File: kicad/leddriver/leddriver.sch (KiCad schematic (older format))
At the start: 7 parts, among them J1 Conn_01x02_Male, J2 Conn_01x01_Male, U1 TLC555xP

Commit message: Add new code
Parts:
- removed J1: Conn_01x02_Male, Connector_PinSocket_2.54mm:PinSocket_1x02_P2.54mm_Vertical, symbol Connector:Conn_01x02_Male
- removed J2: Conn_01x01_Male, Connector_PinHeader_2.54mm:PinHeader_1x01_P2.54mm_Vertical, symbol Connector:Conn_01x01_Male
- added BZ1: Buzzer, Buzzer_Beeper:MagneticBuzzer_ProSignal_ABI-010-RC, symbol Device:Buzzer
- added C3: 4.7uF, Capacitor_THT:C_Disc_D4.3mm_W1.9mm_P5.00mm, symbol Device:C
- added C4: .01uF, Capacitor_THT:C_Disc_D4.3mm_W1.9mm_P5.00mm, symbol Device:C
- added J1, J3: Conn_01x01_Male, Connector_PinHeader_2.54mm:PinHeader_1x01_P2.54mm_Vertical, symbol Connector:Conn_01x01_Male
- added J2: Conn_01x02_Male, Connector_PinSocket_2.54mm:PinSocket_1x02_P2.54mm_Vertical, symbol Connector:Conn_01x02_Male
- added Q1: 2N3904, leddriver:TO-92_HandSolder_Large_Pad, symbol Transistor_BJT:2N3904
- added R3, R5: 68k, Resistor_THT:R_Axial_DIN0204_L3.6mm_D1.6mm_P2.54mm_Vertical, symbol Device:R
- added R4: 1k, Resistor_THT:R_Axial_DIN0204_L3.6mm_D1.6mm_P2.54mm_Vertical, symbol Device:R
- added SW1: SW_Push, Button_Switch_THT:SW_PUSH_6mm_H5mm, symbol Switch:SW_Push
- added U2: TLC555xP, Package_DIP:DIP-8_W7.62mm, symbol Timer:TLC555xP
- C1: value 0.01uF -> 1uF; footprint Capacitor_SMD:C_1206_3216Metric_Pad1.33x1.80mm_HandSolder -> Capacitor_THT:C_Disc_D4.3mm_W1.9mm_P5.00mm
- C2: value 10uF -> .01uF; footprint Capacitor_SMD:C_1206_3216Metric_Pad1.33x1.80mm_HandSolder -> Capacitor_THT:C_Disc_D4.3mm_W1.9mm_P5.00mm
- R1, R2: footprint Resistor_SMD:R_0805_2012Metric_Pad1.20x1.40mm_HandSolder -> Resistor_THT:R_Axial_DIN0204_L3.6mm_D1.6mm_P2.54mm_Vertical
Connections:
- net GND: now also BZ1.2 (+), C3.2, C4.2, J2.2 (Pin_2), R3.2, U2.1 (GND)
- net VCC: now also R2.1, J2.1 (Pin_1), J3.1 (Pin_1), Q1.3 (C), R4.1, U2.8 (VCC)
- net at R2.2, U1.2 (TR), U1.6 (THR): now also R3.1, SW1.2; no longer C2.1
- net OUT1: now reaches U1.3 (Q)
- net OUT1: now also U2.4 (R)
- net at U1.5 (CV): now also C2.1; no longer C1.1
- new net: C1.1, R1.2, SW1.1
- new net: C3.1, R5.2, U2.2 (TR), U2.6 (THR)
- new net: C4.1, U2.5 (CV)
- new net: R4.2, R5.1, U2.7 (DIS)
- new net: BZ1.1 (-), Q1.1 (E)
- new net OUT: J1.1 (Pin_1), Q1.2 (B), U2.3 (Q)
- now unconnected: U1.7 (DIS)
- no-connect marks 0 -> 1
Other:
- moved on the sheet: U1

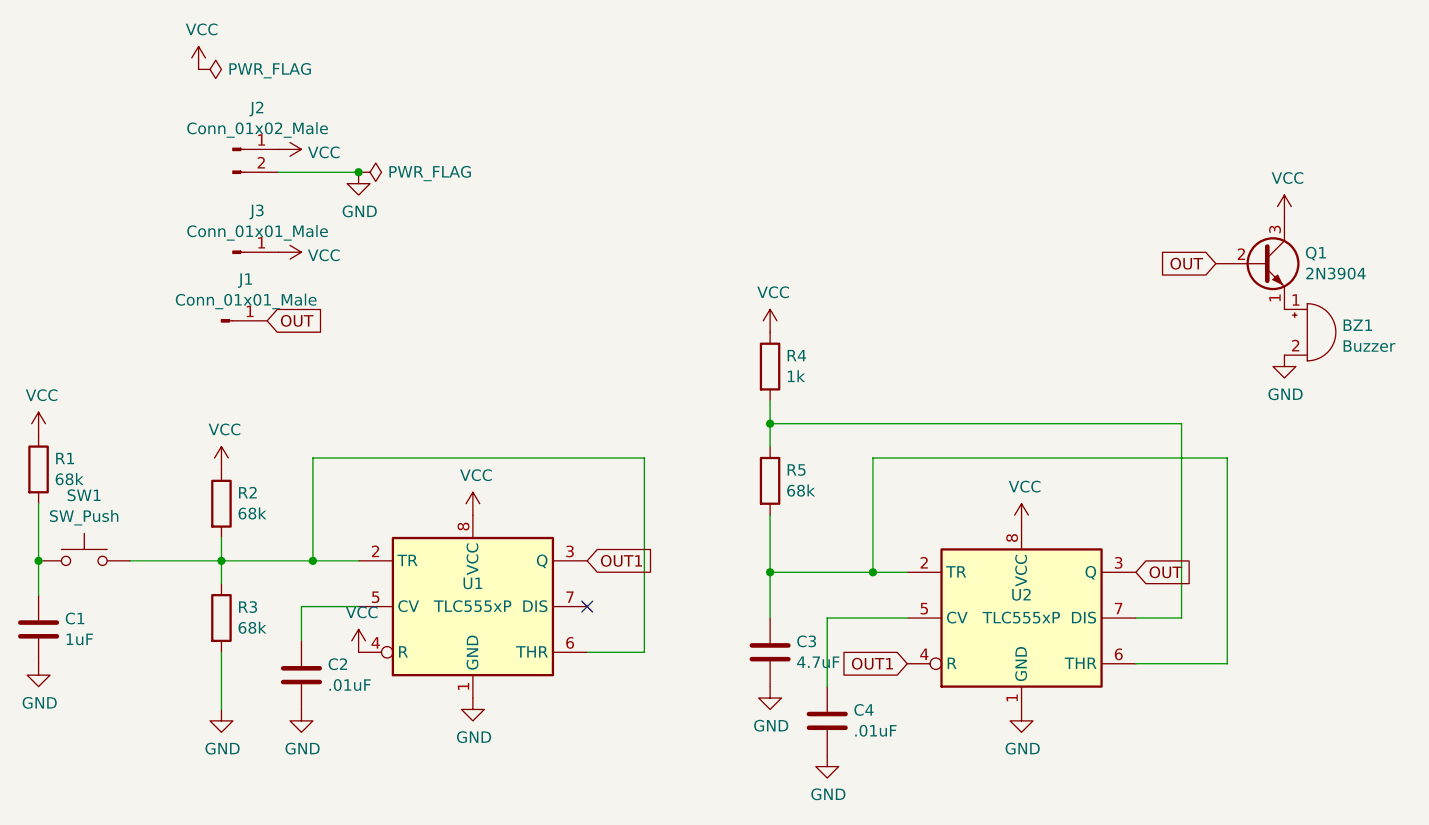
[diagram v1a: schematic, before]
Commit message: Add new led driver schematic
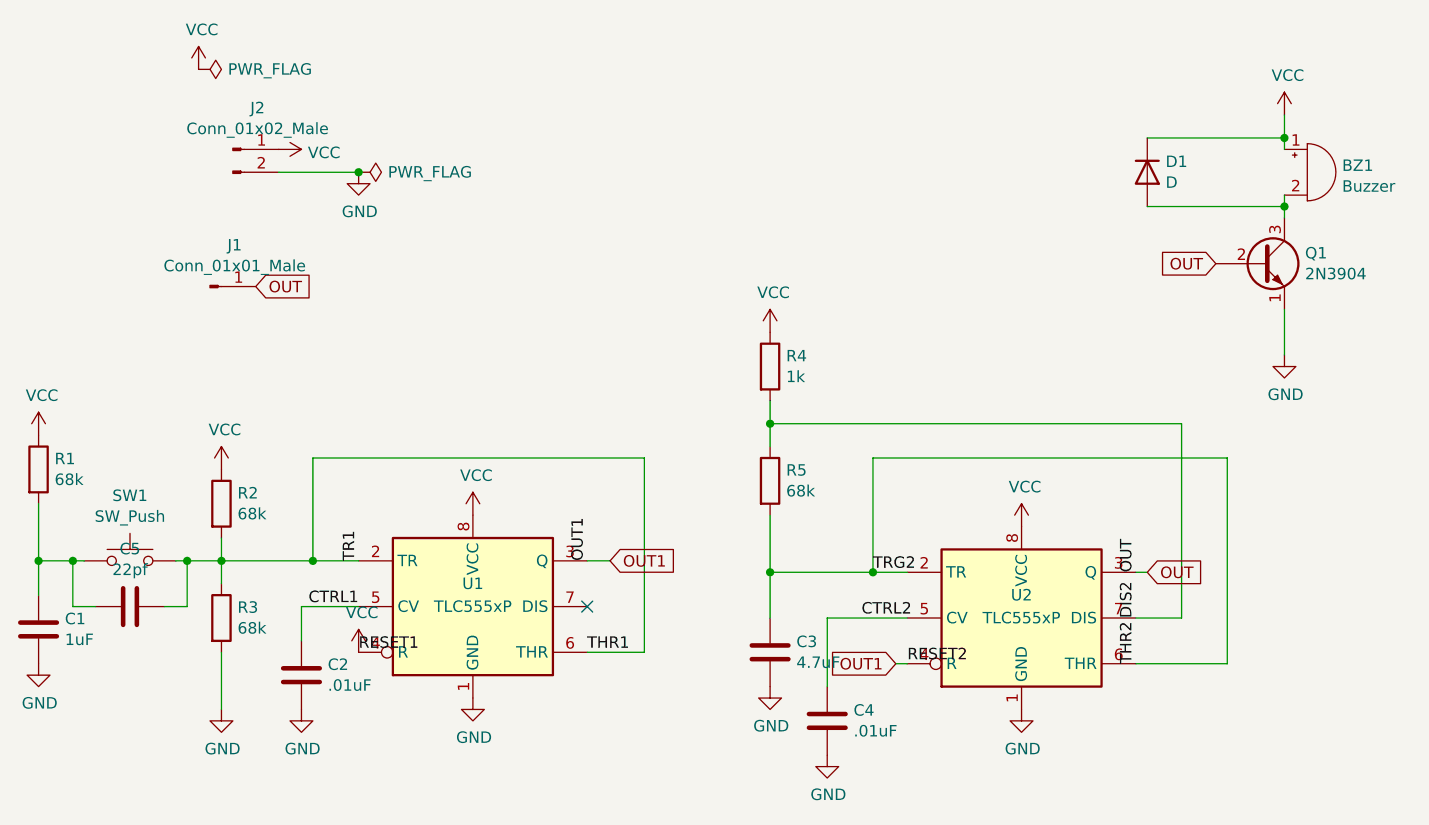
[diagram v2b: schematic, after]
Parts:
- removed J3: Conn_01x01_Male, Connector_PinHeader_2.54mm:PinHeader_1x01_P2.54mm_Vertical, symbol Connector:Conn_01x01_Male
- added C5: 22pf, Capacitor_THT:C_Disc_D3.0mm_W1.6mm_P2.50mm, symbol Device:C
- added D1: D, Diode_THT:D_5KPW_P7.62mm_Vertical_AnodeUp, symbol Device:D
- C1, C2, C3, C4: footprint Capacitor_THT:C_Disc_D4.3mm_W1.9mm_P5.00mm -> Capacitor_THT:C_Radial_D4.0mm_H5.0mm_P1.50mm
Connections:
- net GND: now also Q1.1 (E); no longer BZ1.2 (+)
- net VCC: now also BZ1.1 (-), D1.1 (K); no longer Q1.3 (C)
- net THR1: now reaches R2.2, R3.1, SW1.2, U1.2 (TR), U1.6 (THR)
- net THR1: now also C5.1
- net CTRL1: now reaches C2.1, U1.5 (CV)
- net at C1.1, R1.2, SW1.1: now also C5.2
- net THR2: now reaches C3.1, R5.2, U2.2 (TR), U2.6 (THR)
- net CTRL2: now reaches C4.1, U2.5 (CV)
- net DIS2: now reaches R4.2, R5.1, U2.7 (DIS)
- new net: BZ1.2 (+), D1.2 (A), Q1.3 (C)
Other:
- moved on the sheet: BZ1, J1, SW1
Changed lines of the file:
@@
 F 0 "C1" H 3765 3246 50  0000 L CNN
 F 1 "1uF" H 3765 3155 50  0000 L CNN
-F 2 "Capacitor_THT:C_Disc_D4.3mm_W1.9mm_P5.00mm" H 3688 3050 50  0001 C CNN
+F 2 "Capacitor_THT:C_Radial_D4.0mm_H5.0mm_P1.50mm" H 3688 3050 50  0001 C CNN
 F 3 "~" H 3650 3200 50  0001 C CNN
 	1    3650 3200
@@
 Wire Wire Line
 	4450 2900 4450 3000
-Wire Wire Line
-	4450 2900 4850 2900
 Connection ~ 4850 2900
 $Comp
@@
 Wire Wire Line
 	4700 1200 5050 1200
-Text GLabel 4650 1850 2    50   Input ~ 0
+Text GLabel 4600 1700 2    50   Input ~ 0
 OUT
-Text GLabel 6050 2900 2    50   Input ~ 0
+Text GLabel 6150 2900 2    50   Input ~ 0
 OUT1
 $Comp
@@
 F 0 "C2" H 4915 3446 50  0000 L CNN
 F 1 ".01uF" H 4915 3355 50  0000 L CNN
-F 2 "Capacitor_THT:C_Disc_D4.3mm_W1.9mm_P5.00mm" H 4838 3250 50  0001 C CNN
+F 2 "Capacitor_THT:C_Radial_D4.0mm_H5.0mm_P1.50mm" H 4838 3250 50  0001 C CNN
 F 3 "~" H 4800 3400 50  0001 C CNN
 	1    4800 3400
@@
 	1    0    0    -1
 $EndComp
-Text GLabel 7450 3350 0    50   Input ~ 0
+Text GLabel 7400 3350 0    50   Input ~ 0
 OUT1
 $Comp
@@
 F 0 "C3" H 6965 3346 50  0000 L CNN
 F 1 "4.7uF" H 6965 3255 50  0000 L CNN
-F 2 "Capacitor_THT:C_Disc_D4.3mm_W1.9mm_P5.00mm" H 6888 3150 50  0001 C CNN
+F 2 "Capacitor_THT:C_Radial_D4.0mm_H5.0mm_P1.50mm" H 6888 3150 50  0001 C CNN
 F 3 "~" H 6850 3300 50  0001 C CNN
 	1    6850 3300
@@
 F 0 "C4" H 7215 3646 50  0000 L CNN
 F 1 ".01uF" H 7215 3555 50  0000 L CNN
-F 2 "Capacitor_THT:C_Disc_D4.3mm_W1.9mm_P5.00mm" H 7138 3450 50  0001 C CNN
+F 2 "Capacitor_THT:C_Radial_D4.0mm_H5.0mm_P1.50mm" H 7138 3450 50  0001 C CNN
 F 3 "~" H 7100 3600 50  0001 C CNN
 	1    7100 3600
@@
 Wire Wire Line
 	6850 2300 6850 2400
-Text GLabel 8450 2950 2    50   Input ~ 0
+Text GLabel 8500 2950 2    50   Input ~ 0
 OUT
-Wire Wire Line
-	4050 2900 4450 2900
-Connection ~ 3650 2900
-Wire Wire Line
-	3650 2900 3650 3050
-Wire Wire Line
-	3650 2650 3650 2900
-$Comp
-L Switch:SW_Push SW1
-U 1 1 5F8F5FE1
-P 3850 2900
-F 0 "SW1" H 3850 3185 50  0000 C CNN
-F 1 "SW_Push" H 3850 3094 50  0000 C CNN
-F 2 "Button_Switch_THT:SW_PUSH_6mm_H5mm" H 3850 3100 50  0001 C CNN
-F 3 "~" H 3850 3100 50  0001 C CNN
-	1    3850 2900
-	1    0    0    -1
-$EndComp
 $Comp
 L Connector:Conn_01x02_Male J2
@@
 L Connector:Conn_01x01_Male J1
 U 1 1 5F9568D2
-P 4450 1850
-F 0 "J1" H 4558 2031 50  0000 C CNN
-F 1 "Conn_01x01_Male" H 4558 1940 50  0000 C CNN
-F 2 "Connector_PinHeader_2.54mm:PinHeader_1x01_P2.54mm_Vertical" H 4450 1850 50  0001 C CNN
-F 3 "~" H 4450 1850 50  0001 C CNN
-	1    4450 1850
-	1    0    0    -1
-$EndComp
-$Comp
-L Connector:Conn_01x01_Male J3
-U 1 1 5F9649F6
-P 4500 1550
-F 0 "J3" H 4608 1731 50  0000 C CNN
-F 1 "Conn_01x01_Male" H 4608 1640 50  0000 C CNN
-F 2 "Connector_PinHeader_2.54mm:PinHeader_1x01_P2.54mm_Vertical" H 4500 1550 50  0001 C CNN
-F 3 "~" H 4500 1550 50  0001 C CNN
-	1    4500 1550
+P 4400 1700
+F 0 "J1" H 4508 1881 50  0000 C CNN
+F 1 "Conn_01x01_Male" H 4508 1790 50  0000 C CNN
+F 2 "Connector_PinHeader_2.54mm:PinHeader_1x01_P2.54mm_Vertical" H 4400 1700 50  0001 C CNN
+F 3 "~" H 4400 1700 50  0001 C CNN
+	1    4400 1700
 	1    0    0    -1
 $EndComp
@@
 $EndComp
 $Comp
-L power:VCC #PWR0106
-U 1 1 5F97C45E
-P 4700 1550
-F 0 "#PWR0106" H 4700 1400 50  0001 C CNN
-F 1 "VCC" V 4715 1678 50  0000 L CNN
-F 2 "" H 4700 1550 50  0001 C CNN
-F 3 "" H 4700 1550 50  0001 C CNN
-	1    4700 1550
-	0    1    1    0
-$EndComp
-$Comp
 L power:VCC #PWR0107
 U 1 1 5F97F134
@@
 L Device:Buzzer BZ1
 U 1 1 5F996F1B
-P 9200 1900
-F 0 "BZ1" H 9352 1929 50  0000 L CNN
-F 1 "Buzzer" H 9352 1838 50  0000 L CNN
-F 2 "Buzzer_Beeper:MagneticBuzzer_ProSignal_ABI-010-RC" V 9175 2000 50  0001 C CNN
-F 3 "~" V 9175 2000 50  0001 C CNN
-	1    9200 1900
+P 9200 1200
+F 0 "BZ1" H 9352 1229 50  0000 L CNN
+F 1 "Buzzer" H 9352 1138 50  0000 L CNN
+F 2 "Buzzer_Beeper:MagneticBuzzer_ProSignal_ABI-010-RC" V 9175 1300 50  0001 C CNN
+F 3 "~" V 9175 1300 50  0001 C CNN
+	1    9200 1200
 	1    0    0    -1
 $EndComp
@@
 L power:VCC #PWR0114
 U 1 1 5F9A00D1
-P 9100 1400
-F 0 "#PWR0114" H 9100 1250 50  0001 C CNN
-F 1 "VCC" H 9115 1573 50  0000 C CNN
-F 2 "" H 9100 1400 50  0001 C CNN
-F 3 "" H 9100 1400 50  0001 C CNN
-	1    9100 1400
-	1    0    0    -1
-$EndComp
+P 9100 950
+F 0 "#PWR0114" H 9100 800 50  0001 C CNN
+F 1 "VCC" H 9115 1123 50  0000 C CNN
+F 2 "" H 9100 950 50  0001 C CNN
+F 3 "" H 9100 950 50  0001 C CNN
+	1    9100 950
+	1    0    0    -1
+$EndComp
+Text Label 7300 2950 0    50   ~ 0
+TRG2
+Text Label 7250 3150 0    50   ~ 0
+CTRL2
+Wire Wire Line
+	7400 3350 7450 3350
+Text Label 8450 2950 1    50   ~ 0
+OUT
+Wire Wire Line
+	8450 2950 8500 2950
+Text Label 8450 3150 1    50   ~ 0
+DIS2
+Text Label 8450 3350 1    50   ~ 0
+THR2
+Text Label 5050 2900 1    50   ~ 0
+TR1
+Text Label 7450 3350 0    50   ~ 0
+RESET2
+Text Label 5050 3100 2    50   ~ 0
+CTRL1
+Text Label 5050 3300 0    50   ~ 0
+RESET1
+Text Label 6050 3300 0    50   ~ 0
+THR1
+Text Label 6050 2900 1    50   ~ 0
+OUT1
+Wire Wire Line
+	6050 2900 6150 2900
+Wire Wire Line
+	9100 950  9100 1050
+Wire Wire Line
+	9100 1300 9100 1350
+$Comp
+L Device:D D1
+U 1 1 5F93D059
+P 8500 1200
+F 0 "D1" V 8454 1280 50  0000 L CNN
+F 1 "D" V 8545 1280 50  0000 L CNN
+F 2 "Diode_THT:D_5KPW_P7.62mm_Vertical_AnodeUp" H 8500 1200 50  0001 C CNN
+F 3 "~" H 8500 1200 50  0001 C CNN
+	1    8500 1200
+	0    1    1    0
+$EndComp
+Wire Wire Line
+	8500 1350 9100 1350
+Connection ~ 9100 1350
+Wire Wire Line
+	9100 1350 9100 1400
+Wire Wire Line
+	8500 1050 9100 1050
+Connection ~ 9100 1050
+Wire Wire Line
+	9100 1050 9100 1100
+Wire Wire Line
+	9100 1800 9100 2000
+$Comp
+L Device:C C5
+U 1 1 5F94D72B
+P 4050 3100
+F 0 "C5" V 3798 3100 50  0000 C CNN
+F 1 "22pf" V 3889 3100 50  0000 C CNN
+F 2 "Capacitor_THT:C_Disc_D3.0mm_W1.6mm_P2.50mm" H 4088 2950 50  0001 C CNN
+F 3 "~" H 4050 3100 50  0001 C CNN
+	1    4050 3100
+	0    1    1    0
+$EndComp
+Wire Wire Line
+	4450 2900 4850 2900
+$Comp
+L Switch:SW_Push SW1
+U 1 1 5F8F5FE1
+P 4050 2900
+F 0 "SW1" H 4050 3185 50  0000 C CNN
+F 1 "SW_Push" H 4050 3094 50  0000 C CNN
+F 2 "Button_Switch_THT:SW_PUSH_6mm_H5mm" H 4050 3100 50  0001 C CNN
+F 3 "~" H 4050 3100 50  0001 C CNN
+	1    4050 2900
+	1    0    0    -1
+$EndComp
+Wire Wire Line
+	3650 2650 3650 2900
+Wire Wire Line
+	3650 2900 3800 2900
+Connection ~ 3650 2900
+Wire Wire Line
+	3650 2900 3650 3050
+Wire Wire Line
+	4250 2900 4300 2900
+Wire Wire Line
+	4200 3100 4300 3100
+Wire Wire Line
+	4300 3100 4300 2900
+Connection ~ 4300 2900
+Wire Wire Line
+	4300 2900 4450 2900
+Wire Wire Line
+	3900 3100 3800 3100
+Wire Wire Line
+	3800 3100 3800 2900
+Connection ~ 3800 2900
+Wire Wire Line
+	3800 2900 3850 2900
 $EndSCHEMATC

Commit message: Add change according to 12v test
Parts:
- added R6, R7: 10k, Resistor_THT:R_Axial_DIN0204_L3.6mm_D1.6mm_P2.54mm_Vertical, symbol Device:R
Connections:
- net GND: now also R7.2
- net OUT: now also R6.2; no longer Q1.2 (B)
- new net: Q1.2 (B), R6.1, R7.1
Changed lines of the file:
@@
 	1    0    0    -1
 $EndComp
-Text GLabel 8800 1600 0    50   Input ~ 0
+Text GLabel 8000 1600 0    50   Input ~ 0
 OUT
 $Comp
@@
 	9100 1050 9100 1100
 Wire Wire Line
-	9100 1800 9100 2000
+	9100 1800 9100 1950
 $Comp
 L Device:C C5
@@
 Wire Wire Line
 	3800 2900 3850 2900
+$Comp
+L Device:R R7
+U 1 1 5F947F9D
+P 8550 1750
+F 0 "R7" H 8620 1796 50  0000 L CNN
+F 1 "10k" H 8620 1705 50  0000 L CNN
+F 2 "Resistor_THT:R_Axial_DIN0204_L3.6mm_D1.6mm_P2.54mm_Vertical" V 8480 1750 50  0001 C CNN
+F 3 "~" H 8550 1750 50  0001 C CNN
+	1    8550 1750
+	1    0    0    -1
+$EndComp
+$Comp
+L Device:R R6
+U 1 1 5F949B69
+P 8250 1600
+F 0 "R6" V 8043 1600 50  0000 C CNN
+F 1 "10k" V 8134 1600 50  0000 C CNN
+F 2 "Resistor_THT:R_Axial_DIN0204_L3.6mm_D1.6mm_P2.54mm_Vertical" V 8180 1600 50  0001 C CNN
+F 3 "~" H 8250 1600 50  0001 C CNN
+	1    8250 1600
+	0    1    1    0
+$EndComp
+Wire Wire Line
+	8000 1600 8100 1600
+Wire Wire Line
+	8400 1600 8550 1600
+Wire Wire Line
+	8550 1600 8800 1600
+Connection ~ 8550 1600
+Wire Wire Line
+	8550 1900 8550 1950
+Wire Wire Line
+	8550 1950 9100 1950
+Connection ~ 9100 1950
+Wire Wire Line
+	9100 1950 9100 2000
 $EndSCHEMATC

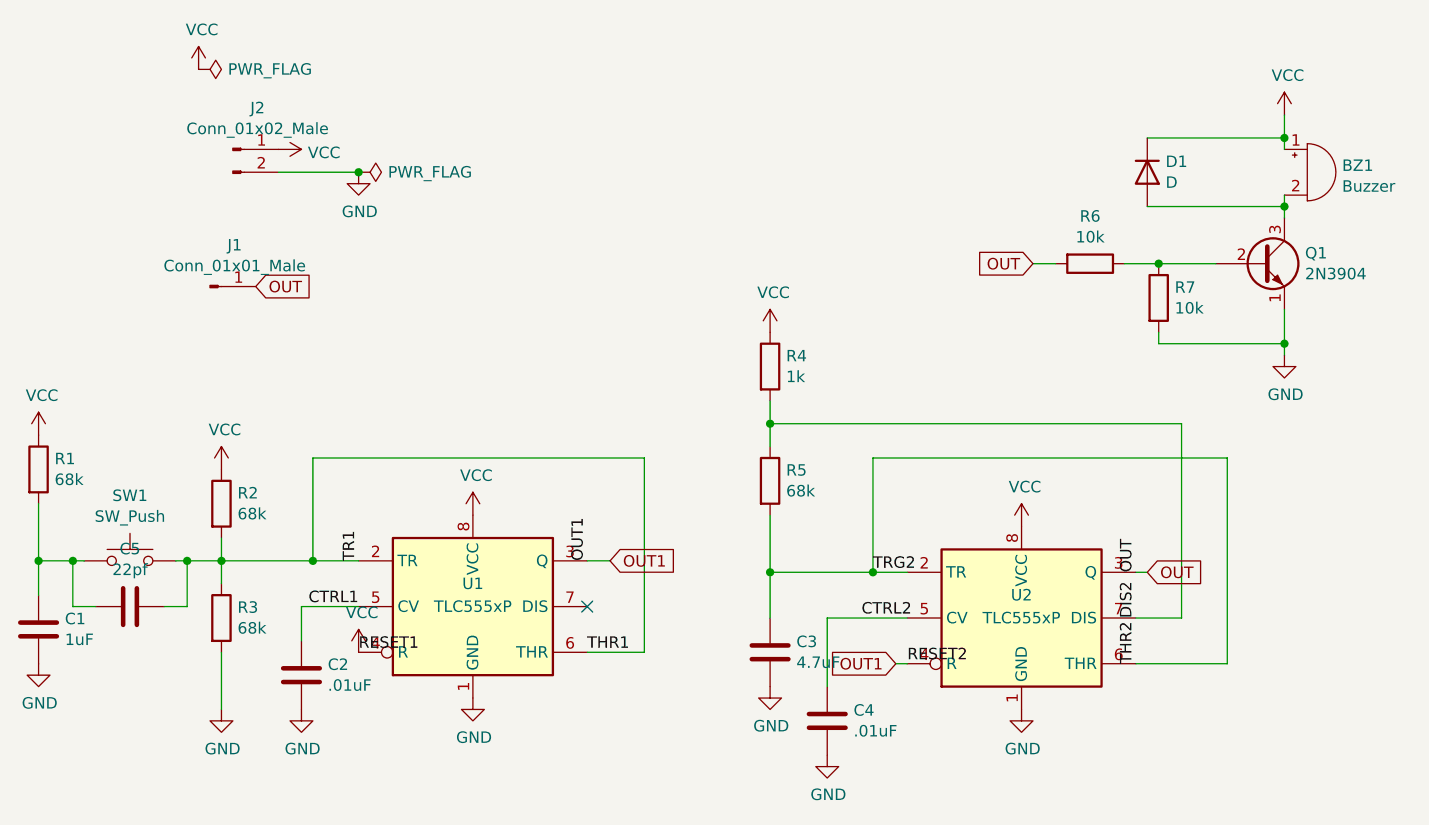
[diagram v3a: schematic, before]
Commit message: improve the current consumption at standby
20mA to 10mA  now
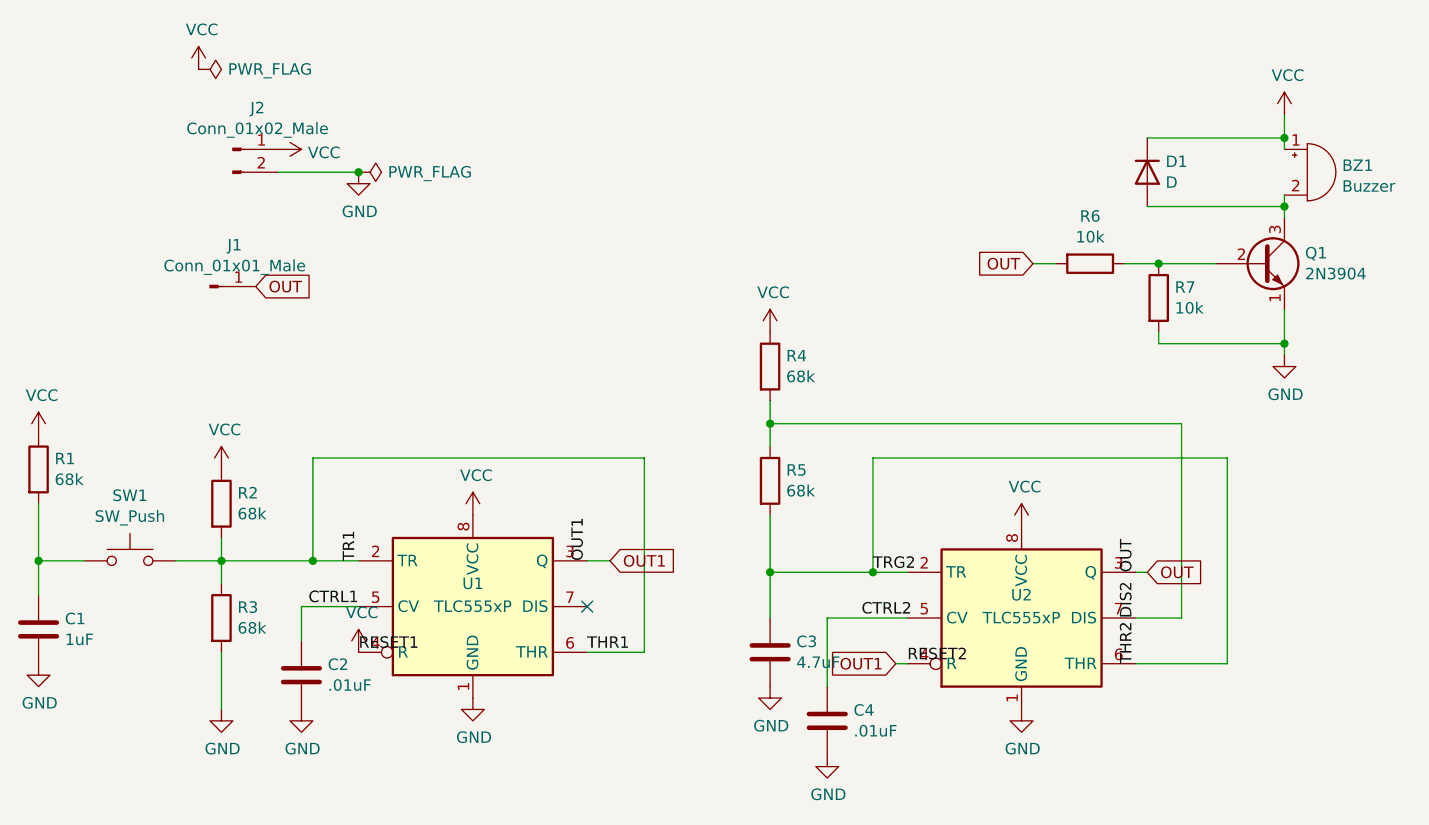
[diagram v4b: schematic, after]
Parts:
- removed C5: 22pf, Capacitor_THT:C_Disc_D3.0mm_W1.6mm_P2.50mm, symbol Device:C
- R4: value 1k -> 68k
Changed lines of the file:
@@
 P 6850 2050
 F 0 "R4" H 6920 2096 50  0000 L CNN
-F 1 "1k" H 6920 2005 50  0000 L CNN
+F 1 "68k" H 6920 2005 50  0000 L CNN
 F 2 "Resistor_THT:R_Axial_DIN0204_L3.6mm_D1.6mm_P2.54mm_Vertical" V 6780 2050 50  0001 C CNN
 F 3 "~" H 6850 2050 50  0001 C CNN
@@
 Wire Wire Line
 	9100 1800 9100 1950
-$Comp
-L Device:C C5
-U 1 1 5F94D72B
-P 4050 3100
-F 0 "C5" V 3798 3100 50  0000 C CNN
-F 1 "22pf" V 3889 3100 50  0000 C CNN
-F 2 "Capacitor_THT:C_Disc_D3.0mm_W1.6mm_P2.50mm" H 4088 2950 50  0001 C CNN
-F 3 "~" H 4050 3100 50  0001 C CNN
-	1    4050 3100
-	0    1    1    0
-$EndComp
 Wire Wire Line
 	4450 2900 4850 2900
@@
 Wire Wire Line
 	3650 2650 3650 2900
-Wire Wire Line
-	3650 2900 3800 2900
 Connection ~ 3650 2900
 Wire Wire Line
 	3650 2900 3650 3050
-Wire Wire Line
-	4250 2900 4300 2900
-Wire Wire Line
-	4200 3100 4300 3100
-Wire Wire Line
-	4300 3100 4300 2900
-Connection ~ 4300 2900
-Wire Wire Line
-	4300 2900 4450 2900
-Wire Wire Line
-	3900 3100 3800 3100
-Wire Wire Line
-	3800 3100 3800 2900
-Connection ~ 3800 2900
-Wire Wire Line
-	3800 2900 3850 2900
 $Comp
 L Device:R R7
@@
 Wire Wire Line
 	9100 1950 9100 2000
+Wire Wire Line
+	4250 2900 4450 2900
+Wire Wire Line
+	3650 2900 3850 2900
 $EndSCHEMATC
